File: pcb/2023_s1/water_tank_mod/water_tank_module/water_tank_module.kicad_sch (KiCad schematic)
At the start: 9 parts

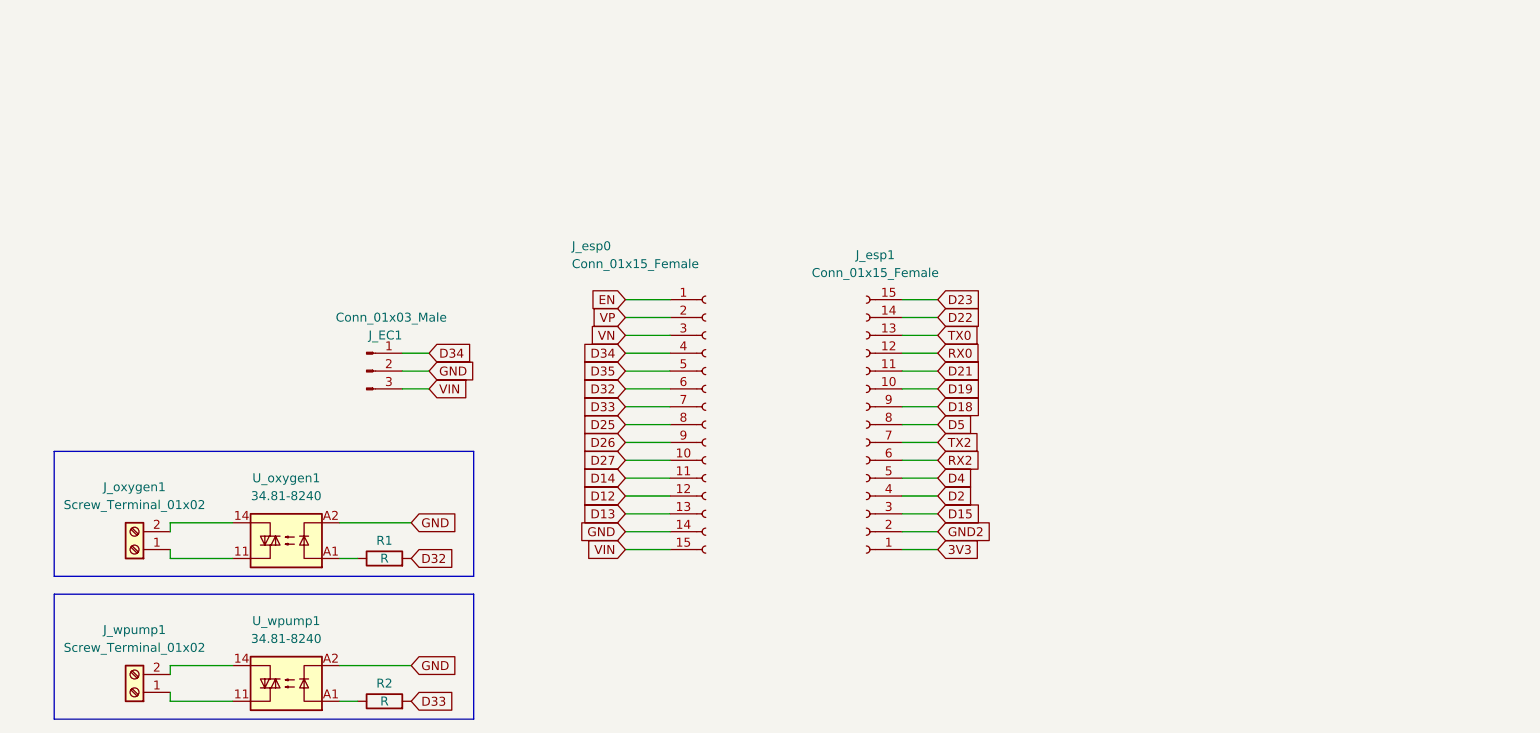
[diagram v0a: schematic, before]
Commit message: water tank update, adn separation into control and power module
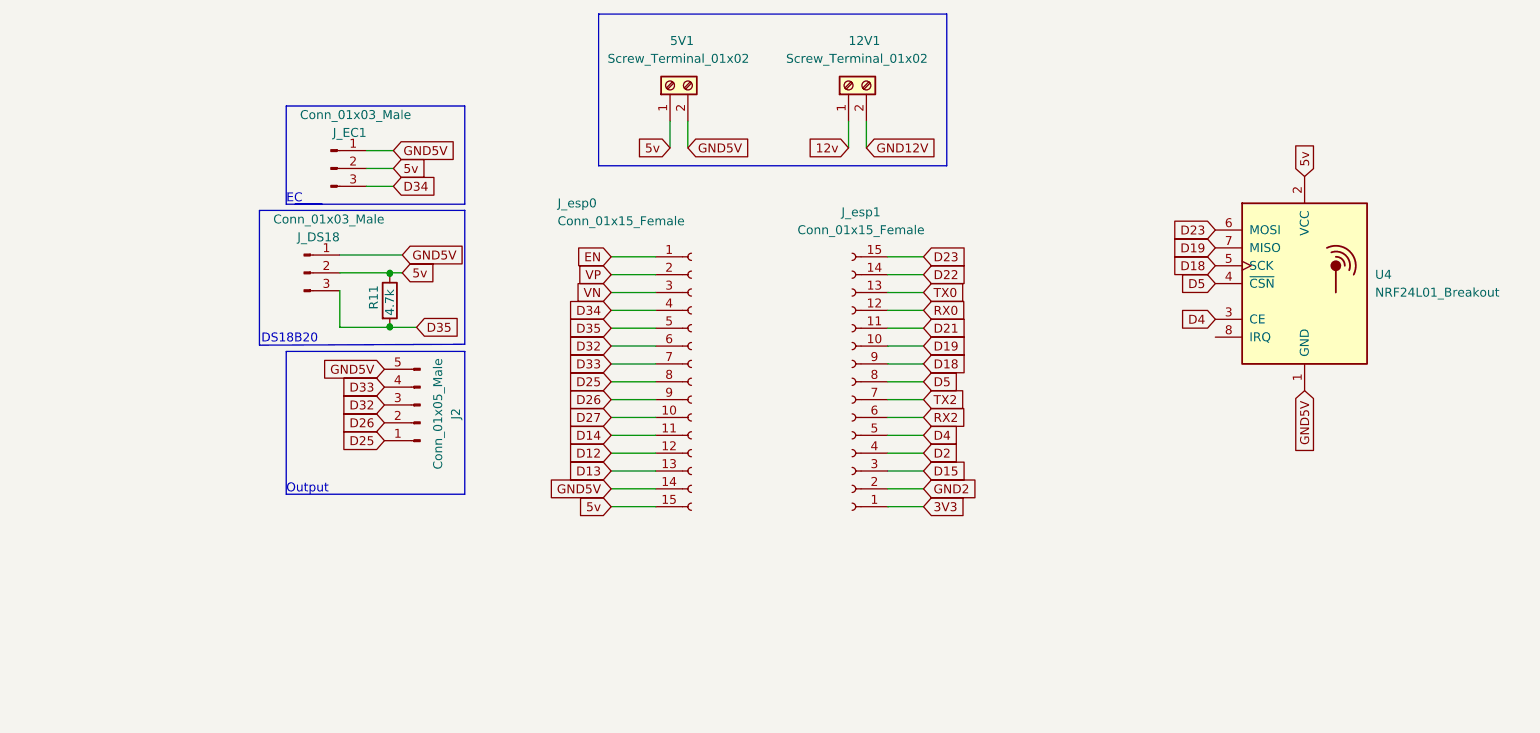
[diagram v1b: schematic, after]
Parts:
- removed J_oxygen1: Screw_Terminal_01x02, symbol Connector:Screw_Terminal_01x02
- removed J_wpump1: Screw_Terminal_01x02, TerminalBlock:TerminalBlock_Altech_AK300-2_P5.00mm, symbol Connector:Screw_Terminal_01x02
- removed R1: R, symbol Device:R
- removed R2: R, Resistor_THT:R_Axial_DIN0204_L3.6mm_D1.6mm_P5.08mm_Vertical, symbol Device:R
- removed U_oxygen1, U_wpump1: 34.81-8240, OptoDevice:Finder_34.81, symbol Relay_SolidState:34.81-8240
- added 12V1, 5V1: Screw_Terminal_01x02, TerminalBlock:TerminalBlock_Altech_AK300-2_P5.00mm, symbol Connector:Screw_Terminal_01x02
- added J2: Conn_01x05_Male, Connector_JST:JST_EH_B5B-EH-A_1x05_P2.50mm_Vertical, symbol Connector:Conn_01x05_Male
- added J_DS18: Conn_01x03_Male, Connector_JST:JST_EH_B3B-EH-A_1x03_P2.50mm_Vertical, symbol Connector:Conn_01x03_Male
- added R11: 4.7k, Resistor_THT:R_Axial_DIN0204_L3.6mm_D1.6mm_P2.54mm_Vertical, symbol Device:R
- added U4: NRF24L01_Breakout, RF_Module:nRF24L01_Breakout, symbol RF:NRF24L01_Breakout
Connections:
- net D18: now also U4.5 (SCK)
- net D19: now also U4.7 (MISO)
- net D23: now also U4.6 (MOSI)
- net D25: now also J2.1 (Pin_1)
- net D26: now also J2.2 (Pin_2)
- net D32: now also J2.3 (Pin_3)
- net D33: now also J2.4 (Pin_4)
- net D34: now also J_EC1.3 (Pin_3); no longer J_EC1.1 (Pin_1)
- net D35: now also J_DS18.3 (Pin_3), R11.2
- net D4: now also U4.3 (CE)
- net D5: now also U4.4 (~{CSN})
- net GND renamed 5v
- net 5v: now also J_esp0.15 (Pin_15), 5V1.1 (Pin_1), J_DS18.2 (Pin_2), R11.1, U4.2 (VCC); no longer J_esp0.14 (Pin_14)
- removed net VIN: J_EC1.3 (Pin_3), J_esp0.15 (Pin_15)
- new net 12v: 12V1.1 (Pin_1)
- new net GND12V: 12V1.2 (Pin_2)
- new net GND5V: 5V1.2 (Pin_2), J2.5 (Pin_5), J_DS18.1 (Pin_1), J_EC1.1 (Pin_1), J_esp0.14 (Pin_14), U4.1 (GND)
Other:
- note added: "DS18B20"
- note added: "EC"
- note added: "Output"
- moved on the sheet: J_EC1, J_esp0, J_esp1

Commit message: update, added 3d shapes for the pieces, and added capacitor
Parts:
- removed 12V1: Screw_Terminal_01x02, TerminalBlock:TerminalBlock_Altech_AK300-2_P5.00mm, symbol Connector:Screw_Terminal_01x02
- added C1: C_Polarized, symbol Device:C_Polarized
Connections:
- net 5v: now also C1.1
- net GND5V: now also C1.2
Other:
- moved on the sheet: 5V1, J_esp0, J_esp1

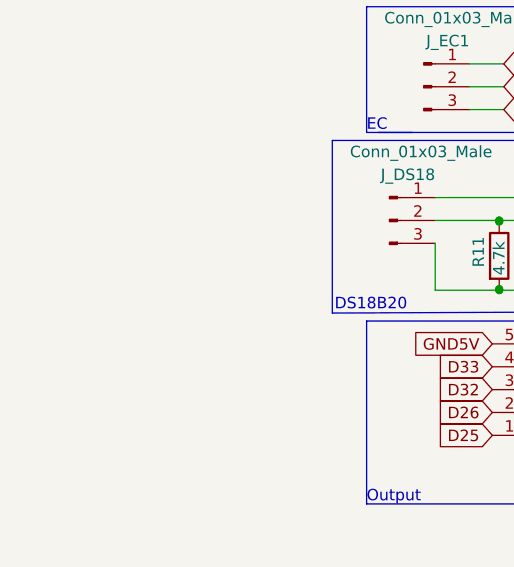
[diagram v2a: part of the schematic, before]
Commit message: update, added mounting holes
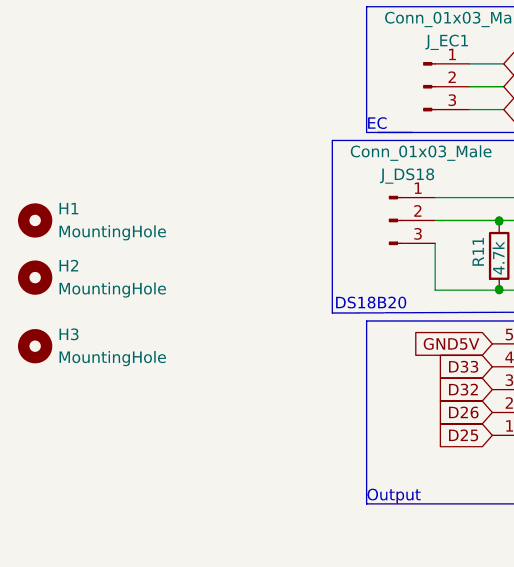
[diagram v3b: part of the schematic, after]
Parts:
- added H1, H2, H3: MountingHole, MountingHole:MountingHole_2.7mm_M2.5_Pad, symbol Mechanical:MountingHole
- C1: footprint (none) -> Capacitor_THT:CP_Radial_D5.0mm_P2.50mm
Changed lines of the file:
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@@
     (property "Reference" "C1" (id 0) (at 141.351 31.75 90))
     (property "Value" "C_Polarized" (id 1) (at 141.351 34.29 90))
-    (property "Footprint" "" (id 2) (at 146.05 38.4048 0)
+    (property "Footprint" "Capacitor_THT:CP_Radial_D5.0mm_P2.50mm" (id 2) (at 146.05 38.4048 0)
       (effects (font (size 1.27 1.27)) hide)
     )
@@
     (pin "3")
   )
+  (symbol (lib_id "Mechanical:MountingHole") (at 39.37 59.69 0) (unit 1)
+    (in_bom yes) (on_board yes) (fields_autoplaced)
+    (property "Reference" "H2" (id 0) (at 41.91 58.4199 0)
+      (effects (font (size 1.27 1.27)) (justify left))
+    )
+    (property "Value" "MountingHole" (id 1) (at 41.91 60.9599 0)
+      (effects (font (size 1.27 1.27)) (justify left))
+    )
+    (property "Footprint" "MountingHole:MountingHole_2.7mm_M2.5_Pad" (id 2) (at 39.37 59.69 0)
+      (effects (font (size 1.27 1.27)) hide)
+    )
+    (property "Datasheet" "~" (id 3) (at 39.37 59.69 0)
+      (effects (font (size 1.27 1.27)) hide)
+    )
+  )
   (symbol (lib_id "Connector:Conn_01x15_Female") (at 157.48 87.63 180) (unit 1)
     (in_bom yes) (on_board yes)
@@
     (pin "8")
     (pin "9")
+  )
+  (symbol (lib_id "Mechanical:MountingHole") (at 39.37 67.31 0) (unit 1)
+    (in_bom yes) (on_board yes) (fields_autoplaced)
+    (property "Reference" "H3" (id 0) (at 41.91 66.0399 0)
+      (effects (font (size 1.27 1.27)) (justify left))
+    )
+    (property "Value" "MountingHole" (id 1) (at 41.91 68.5799 0)
+      (effects (font (size 1.27 1.27)) (justify left))
+    )
+    (property "Footprint" "MountingHole:MountingHole_2.7mm_M2.5_Pad" (id 2) (at 39.37 67.31 0)
+      (effects (font (size 1.27 1.27)) hide)
+    )
+    (property "Datasheet" "~" (id 3) (at 39.37 67.31 0)
+      (effects (font (size 1.27 1.27)) hide)
+    )
+  )
+  (symbol (lib_id "Mechanical:MountingHole") (at 39.37 53.34 0) (unit 1)
+    (in_bom yes) (on_board yes) (fields_autoplaced)
+    (property "Reference" "H1" (id 0) (at 41.91 52.0699 0)
+      (effects (font (size 1.27 1.27)) (justify left))
+    )
+    (property "Value" "MountingHole" (id 1) (at 41.91 54.6099 0)
+      (effects (font (size 1.27 1.27)) (justify left))
+    )
+    (property "Footprint" "MountingHole:MountingHole_2.7mm_M2.5_Pad" (id 2) (at 39.37 53.34 0)
+      (effects (font (size 1.27 1.27)) hide)
+    )
+    (property "Datasheet" "~" (id 3) (at 39.37 53.34 0)
+      (effects (font (size 1.27 1.27)) hide)
+    )
   )
   (symbol (lib_id "Device:R") (at 90.932 57.277 0) (unit 1)
@@
       (reference "C1") (unit 1) (value "C_Polarized") (footprint "Capacitor_THT:CP_Radial_D5.0mm_P2.50mm")
     )
+    (path "/fa25a304-d13e-45d9-8a6b-42fa3ef07e17"
+      (reference "H1") (unit 1) (value "MountingHole") (footprint "MountingHole:MountingHole_2.7mm_M2.5_Pad")
+    )
+    (path "/a375cb48-32a6-4fea-8d6b-7fa179ddb707"
+      (reference "H2") (unit 1) (value "MountingHole") (footprint "MountingHole:MountingHole_2.7mm_M2.5_Pad")
+    )
+    (path "/eb25c250-7a5d-4a9a-839e-da707c6768fb"
+      (reference "H3") (unit 1) (value "MountingHole") (footprint "MountingHole:MountingHole_2.7mm_M2.5_Pad")
+    )
     (path "/6ee81dda-a686-46e6-8cf2-3d80448ed171"

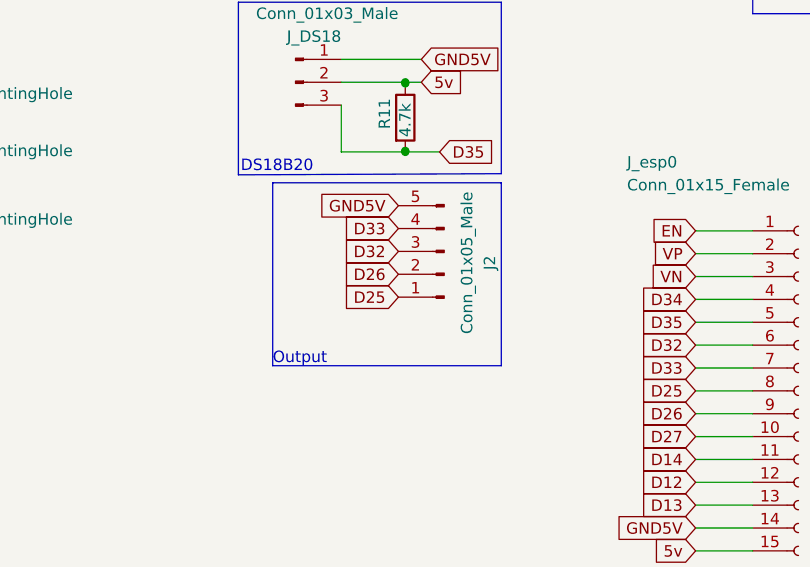
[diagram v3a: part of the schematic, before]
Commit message: update, finished connecting the power pcb module, and added the fan control to both pcbs
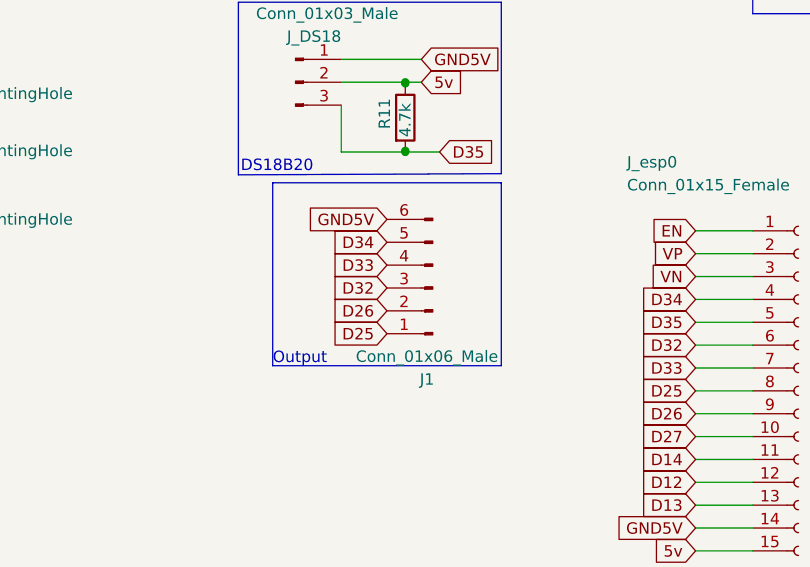
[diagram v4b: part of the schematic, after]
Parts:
- removed J2: Conn_01x05_Male, Connector_JST:JST_EH_B5B-EH-A_1x05_P2.50mm_Vertical, symbol Connector:Conn_01x05_Male
- added J1: Conn_01x06_Male, Connector_JST:JST_EH_B6B-EH-A_1x06_P2.50mm_Vertical, symbol Connector:Conn_01x06_Male
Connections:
- net D25: now also J1.1 (Pin_1)
- net D26: now also J1.2 (Pin_2)
- net D32: now also J1.3 (Pin_3)
- net D33: now also J1.4 (Pin_4)
- net D34: now also J1.5 (Pin_5)
- net GND5V: now also J1.6 (Pin_6)
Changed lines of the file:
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@@
     )
   )
-  (global_label "D26" (shape input) (at 90.17 74.676 180) (fields_autoplaced)
-    (effects (font (size 1.27 1.27)) (justify right))
-    (property "Intersheet References" "${INTERSHEET_REFS}" (id 0) (at 84.0679 74.5966 0)
+  (global_label "D26" (shape input) (at 88.9 78.74 180) (fields_autoplaced)
+    (effects (font (size 1.27 1.27)) (justify right))
+    (property "Intersheet References" "${INTERSHEET_REFS}" (id 0) (at 82.7979 78.6606 0)
       (effects (font (size 1.27 1.27)) (justify right) hide)
     )
@@
     )
   )
-  (global_label "GND5V" (shape input) (at 90.17 67.056 180) (fields_autoplaced)
-    (effects (font (size 1.27 1.27)) (justify right))
-    (property "Intersheet References" "${INTERSHEET_REFS}" (id 0) (at 81.5883 67.1354 0)
+  (global_label "GND5V" (shape input) (at 88.9 68.58 180) (fields_autoplaced)
+    (effects (font (size 1.27 1.27)) (justify right))
+    (property "Intersheet References" "${INTERSHEET_REFS}" (id 0) (at 80.3183 68.6594 0)
       (effects (font (size 1.27 1.27)) (justify right) hide)
     )
@@
     )
   )
-  (global_label "D33" (shape input) (at 90.17 69.596 180) (fields_autoplaced)
-    (effects (font (size 1.27 1.27)) (justify right))
-    (property "Intersheet References" "${INTERSHEET_REFS}" (id 0) (at 84.0679 69.6754 0)
+  (global_label "D33" (shape input) (at 88.9 73.66 180) (fields_autoplaced)
+    (effects (font (size 1.27 1.27)) (justify right))
+    (property "Intersheet References" "${INTERSHEET_REFS}" (id 0) (at 82.7979 73.7394 0)
       (effects (font (size 1.27 1.27)) (justify right) hide)
     )
@@
     )
   )
-  (global_label "D25" (shape input) (at 90.17 77.216 180) (fields_autoplaced)
-    (effects (font (size 1.27 1.27)) (justify right))
-    (property "Intersheet References" "${INTERSHEET_REFS}" (id 0) (at 84.0679 77.1366 0)
+  (global_label "D25" (shape input) (at 88.9 81.28 180) (fields_autoplaced)
+    (effects (font (size 1.27 1.27)) (justify right))
+    (property "Intersheet References" "${INTERSHEET_REFS}" (id 0) (at 82.7979 81.2006 0)
       (effects (font (size 1.27 1.27)) (justify right) hide)
     )
@@
     )
   )
+  (global_label "D34" (shape input) (at 88.9 71.12 180) (fields_autoplaced)
+    (effects (font (size 1.27 1.27)) (justify right))
+    (property "Intersheet References" "${INTERSHEET_REFS}" (id 0) (at 82.7979 71.0406 0)
+      (effects (font (size 1.27 1.27)) (justify right) hide)
+    )
+  )
   (global_label "GND5V" (shape input) (at 91.44 35.941 0) (fields_autoplaced)
     (effects (font (size 1.27 1.27)) (justify left))
@@
     )
   )
-  (global_label "D32" (shape input) (at 90.17 72.136 180) (fields_autoplaced)
-    (effects (font (size 1.27 1.27)) (justify right))
-    (property "Intersheet References" "${INTERSHEET_REFS}" (id 0) (at 84.0679 72.0566 0)
+  (global_label "D32" (shape input) (at 88.9 76.2 180) (fields_autoplaced)
+    (effects (font (size 1.27 1.27)) (justify right))
+    (property "Intersheet References" "${INTERSHEET_REFS}" (id 0) (at 82.7979 76.1206 0)
       (effects (font (size 1.27 1.27)) (justify right) hide)
     )
@@
       (effects (font (size 1.27 1.27)) (justify right) hide)
     )
+  )
+  (symbol (lib_id "Connector:Conn_01x06_Male") (at 93.98 76.2 180) (unit 1)
+    (in_bom yes) (on_board yes) (fields_autoplaced)
+    (property "Reference" "J1" (id 0) (at 93.345 86.36 0))
+    (property "Value" "Conn_01x06_Male" (id 1) (at 93.345 83.82 0))
+    (property "Footprint" "Connector_JST:JST_EH_B6B-EH-A_1x06_P2.50mm_Vertical" (id 2) (at 93.98 76.2 0)
+      (effects (font (size 1.27 1.27)) hide)
+    )
+    (property "Datasheet" "~" (id 3) (at 93.98 76.2 0)
+      (effects (font (size 1.27 1.27)) hide)
+    )
+    (pin "1")
+    (pin "2")
+    (pin "3")
+    (pin "4")
+    (pin "5")
+    (pin "6")
   )
   (symbol (lib_id "Connector:Conn_01x03_Male") (at 82.55 38.481 0) (unit 1)
@@
     (pin "9")
   )
-  (symbol (lib_id "Connector:Conn_01x05_Male") (at 95.25 72.136 180) (unit 1)
-    (in_bom yes) (on_board yes)
-    (property "Reference" "J2" (id 0) (at 100.33 73.406 90))
-    (property "Value" "Conn_01x05_Male" (id 1) (at 97.79 73.406 90))
-    (property "Footprint" "Connector_JST:JST_EH_B5B-EH-A_1x05_P2.50mm_Vertical" (id 2) (at 95.25 72.136 0)
-      (effects (font (size 1.27 1.27)) hide)
-    )
-    (property "Datasheet" "~" (id 3) (at 95.25 72.136 0)
-      (effects (font (size 1.27 1.27)) hide)
-    )
-    (pin "1")
-    (pin "2")
-    (pin "3")
-    (pin "4")
-    (pin "5")
-  )
   (symbol (lib_id "RF:NRF24L01_Breakout") (at 221.107 54.864 0) (unit 1)
     (in_bom yes) (on_board yes) (fields_autoplaced)
@@
       (reference "H3") (unit 1) (value "MountingHole") (footprint "MountingHole:MountingHole_2.7mm_M2.5_Pad")
     )
-    (path "/6ee81dda-a686-46e6-8cf2-3d80448ed171"
-      (reference "J2") (unit 1) (value "Conn_01x05_Male") (footprint "Connector_JST:JST_EH_B5B-EH-A_1x05_P2.50mm_Vertical")
+    (path "/05f4494b-5779-46e5-8ae9-0f5ec633c154"
+      (reference "J1") (unit 1) (value "Conn_01x06_Male") (footprint "Connector_JST:JST_EH_B6B-EH-A_1x06_P2.50mm_Vertical")
     )
     (path "/977a8c43-25e0-4675-a166-3f6d7cf1e985"

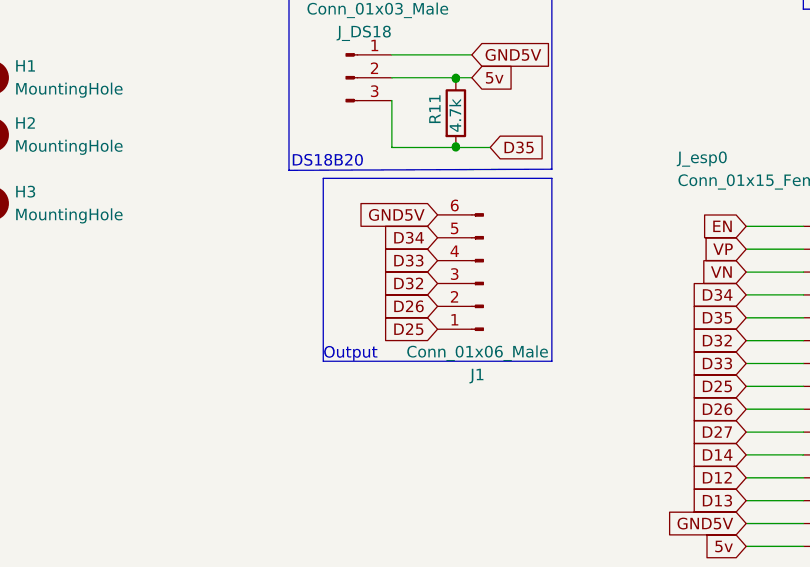
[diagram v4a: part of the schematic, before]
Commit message: fix, fixed positioning of esp32, it was mirrored
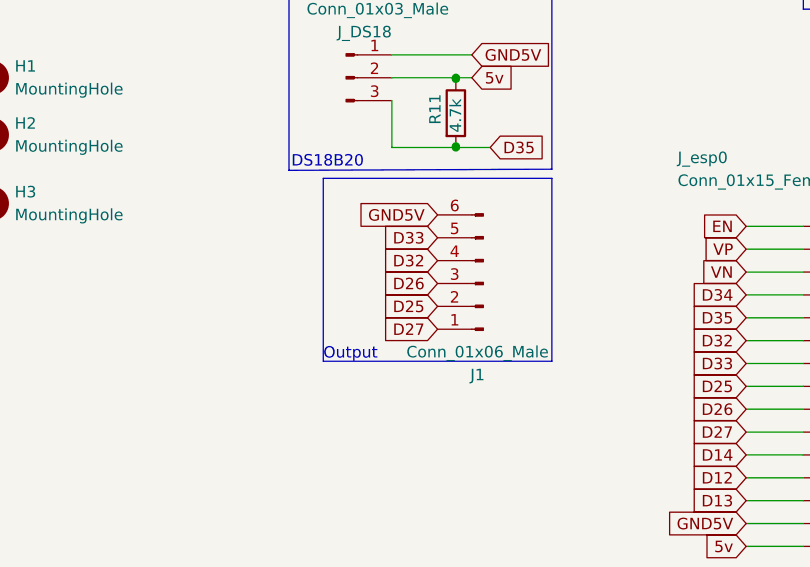
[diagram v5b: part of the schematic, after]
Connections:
- net D25: now also J1.2 (Pin_2); no longer J1.1 (Pin_1)
- net D26: now also J1.3 (Pin_3); no longer J1.2 (Pin_2)
- net D27: now also J1.1 (Pin_1)
- net D32: now also J1.4 (Pin_4); no longer J1.3 (Pin_3)
- net D33: now also J1.5 (Pin_5); no longer J1.4 (Pin_4)
- net D34: no longer J1.5 (Pin_5)
